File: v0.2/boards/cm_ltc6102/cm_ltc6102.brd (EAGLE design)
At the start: 53.2 x 32 mm, 93 parts, among them J1 10118194-0001LF, U1 ADA4528-2ARMZ-R7, U10 TS5A3159ADBVRDBV6-M, U2 LTC6102IMS8PBF, U3 ADM7170ACPZ-1.3-R7CP_8_21-M, U4 MIC2250-1YD5TSOT-23-5_D5-M, U5 INA226_DGS_10DGS10-M, U6 TS3A4751PWRPW14-M, U7 TS5A4624DCKRDCK6-M, X1 PN87520-S

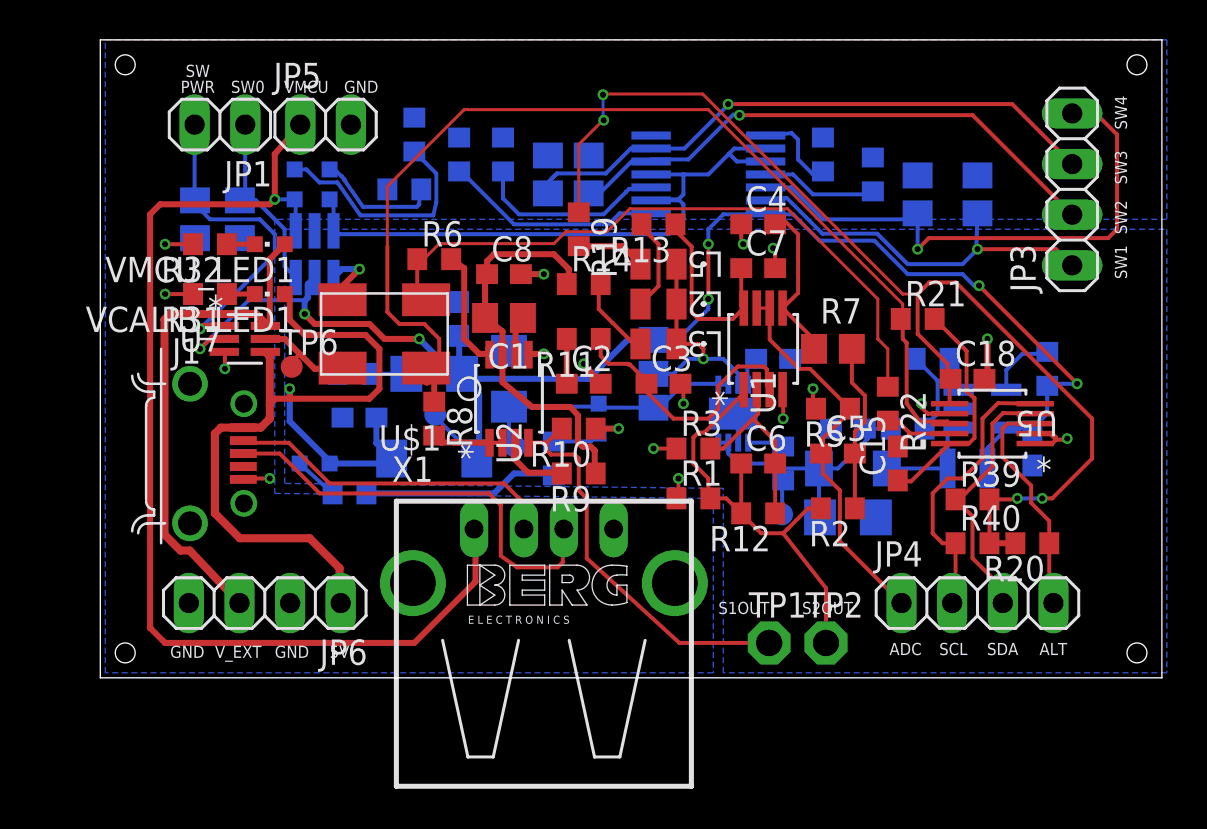
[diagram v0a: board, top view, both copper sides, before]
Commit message: cm_ltc6102: add dgnd and agnd connection, fix silk-screen
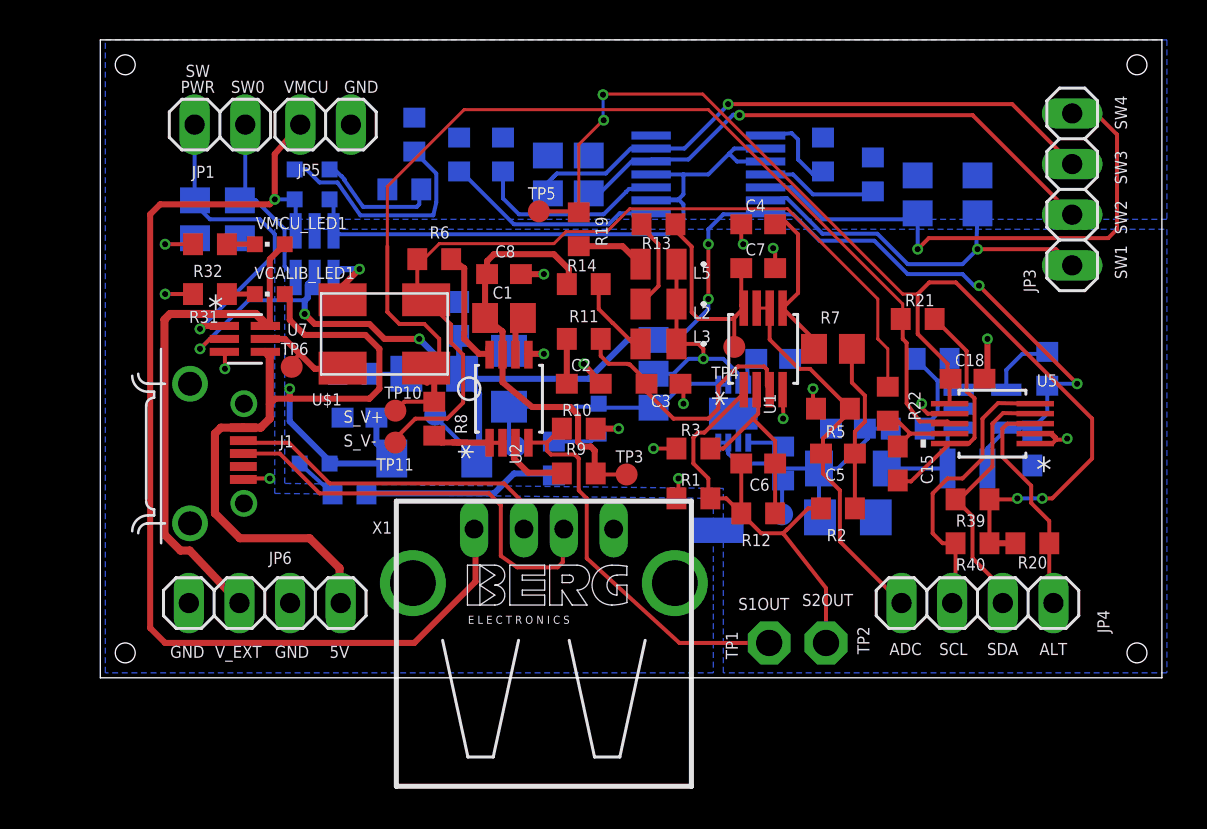
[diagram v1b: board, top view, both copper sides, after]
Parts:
- added SH1: SHORT-VT5, shorts-old:SHORT_TOP-50
- added TP10, TP11, TP3, TP4, TP5: TPTP11R, testpad:TP11R
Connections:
- net ADA_VCC: now also TP4.TP
- net DGND: now also SH1.2
- net GND: now also SH1.1
- net INA_VCC: now also TP5.TP
- net LTC_VCC: now also TP3.TP
- net SHUNT_V+: now also TP10.TP
- net SHUNT_V-: now also TP11.TP
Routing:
- net SHUNT_V-: track 32.8 -> 43.1 mm
- net SHUNT_V+: track 53.1 -> 55.3 mm
- net INA_VCC: track 55.9 -> 57.9 mm
- net LTC_VCC: track 20.6 -> 22.2 mm
- net ADA_VCC: track 9.88 -> 11.5 mm
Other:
- board text added: "S_V+"
- board text added: "S_V-"

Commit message: fix some missing gnd wires
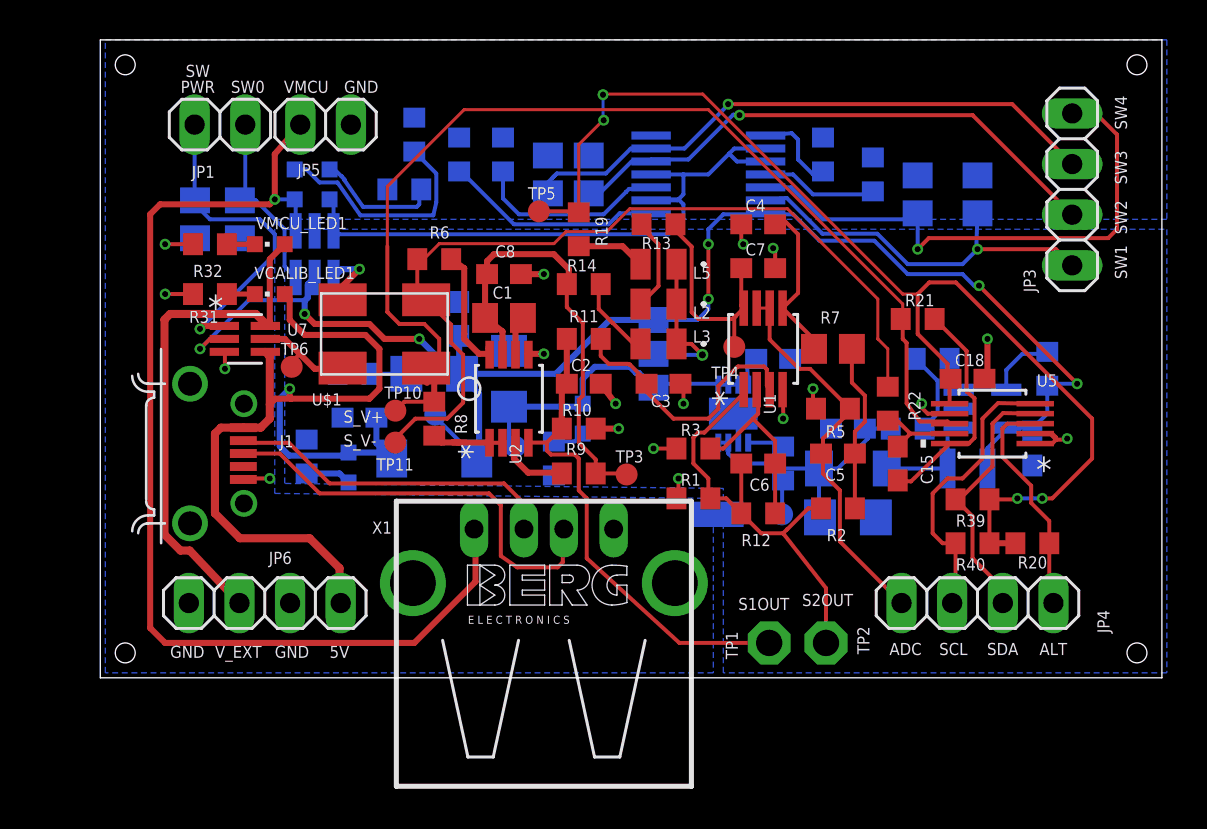
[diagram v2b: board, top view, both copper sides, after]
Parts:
- moved R27 2.84 mm to (10.3, 11.1), turned to 90 degrees
- moved USB_LED 1.71 mm to (12.4, 10.6), turned to 180 degrees
- moved JMP1 1.00 mm to (27.8, 16.2)
- moved 5V_LED 0.80 mm to (24.2, 13.0)
- moved SH1 0.80 mm to (31.0, 8.20)
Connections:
- removed net LTC_OUT: C2.1, R11.2
- removed net N$4: R27.2, R28.2
- net 5V: no longer U3.3
- net 5V_R: now also U3.3
- net GND: now also R27.2, R28.2
- net S1_OUT: now also C2.1, R11.2
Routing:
- net N$4: track 10.0 -> 0.00 mm
- net S1_OUT: track 20.1 -> 25.5 mm
- net 5V: track 11.6 -> 8.00 mm
- net LTC_OUT: track 2.25 -> 0.00 mm
- net 5V_R: track 14.0 -> 15.8 mm
- net 5V_USB: track 45.1 -> 46.3 mm
- net LTC_VCC: track 22.2 -> 23.0 mm
- net N$22: track 2.41 -> 1.61 mm
